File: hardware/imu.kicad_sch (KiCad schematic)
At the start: 4 parts, among them U2 BMI270

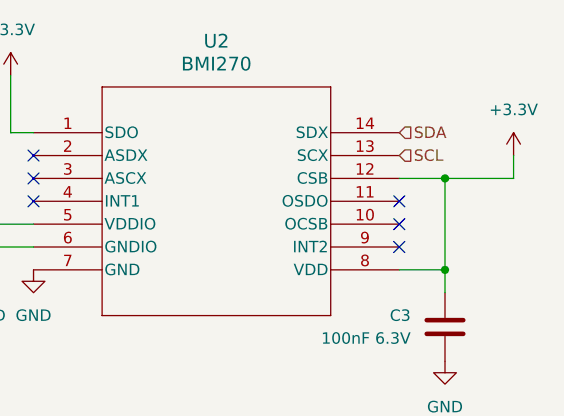
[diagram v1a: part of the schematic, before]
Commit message: lcd wires, wire direction
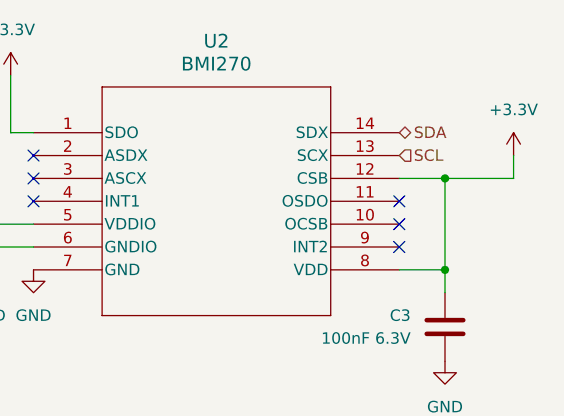
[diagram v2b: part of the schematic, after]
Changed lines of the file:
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@@
 	)
 	(hierarchical_label "SDA"
-		(shape input)
+		(shape bidirectional)
 		(at 177.8 82.55 0)
 		(fields_autoplaced yes)

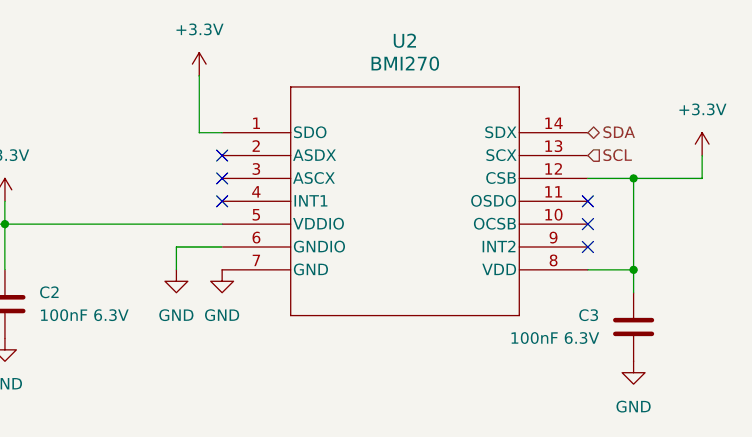
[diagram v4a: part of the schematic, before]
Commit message: Route all board
Fix CS missing for SD card
Add IMU symbol and footprint to the project lib
Finish esp32 pinswaps
Move non critical signals to the keyboard IO expander
Add power flag symbols
Fix Dpad pin type
Fix IMU pin type
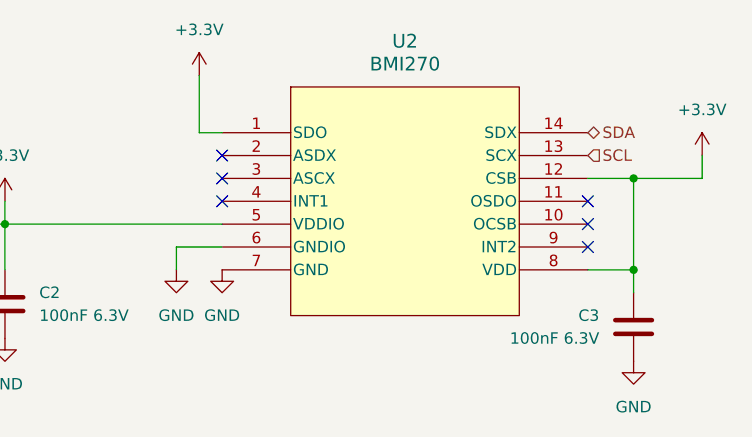
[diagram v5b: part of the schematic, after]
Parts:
- U2: footprint footprints:BMI270_BOS -> badge:BMI270_BOS; symbol 2024-05-01_14-00-02:BMI270 -> badge:BMI270
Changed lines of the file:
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@@
 	)
 	(symbol
-		(lib_id "2024-05-01_14-00-02:BMI270")
-		(at 137.16 82.55 0)
+		(lib_id "badge:BMI270")
+		(at 157.48 90.17 0)
 		(unit 1)
 		(exclude_from_sim no)
@@
 			)
 		)
-		(property "Footprint" "footprints:BMI270_BOS"
+		(property "Footprint" "badge:BMI270_BOS"
 			(at 137.16 82.55 0)
 			(effects

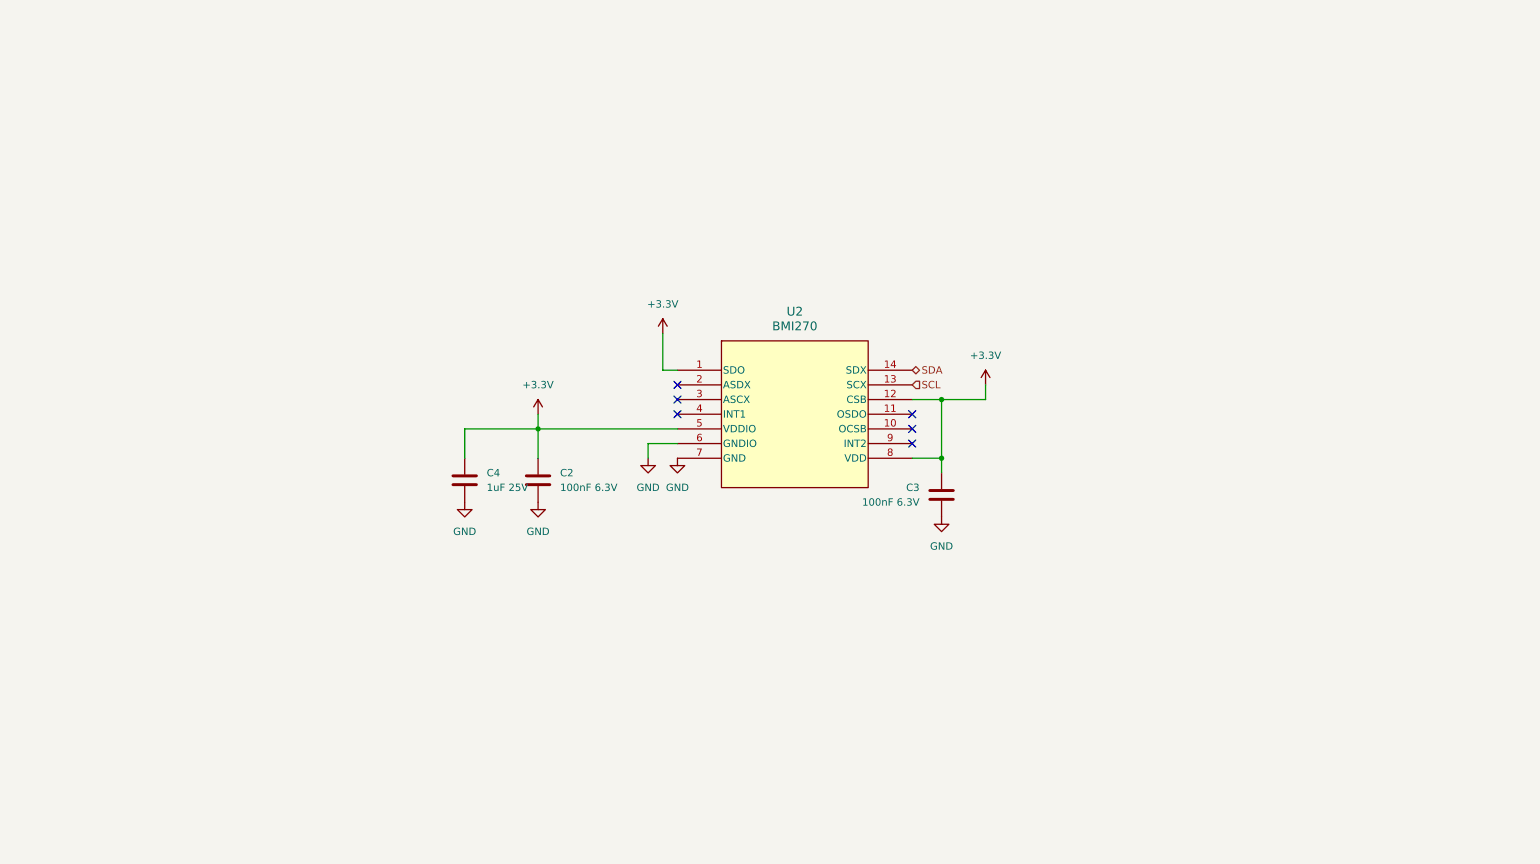
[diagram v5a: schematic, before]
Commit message: Beautified schematic, added I2C addresses
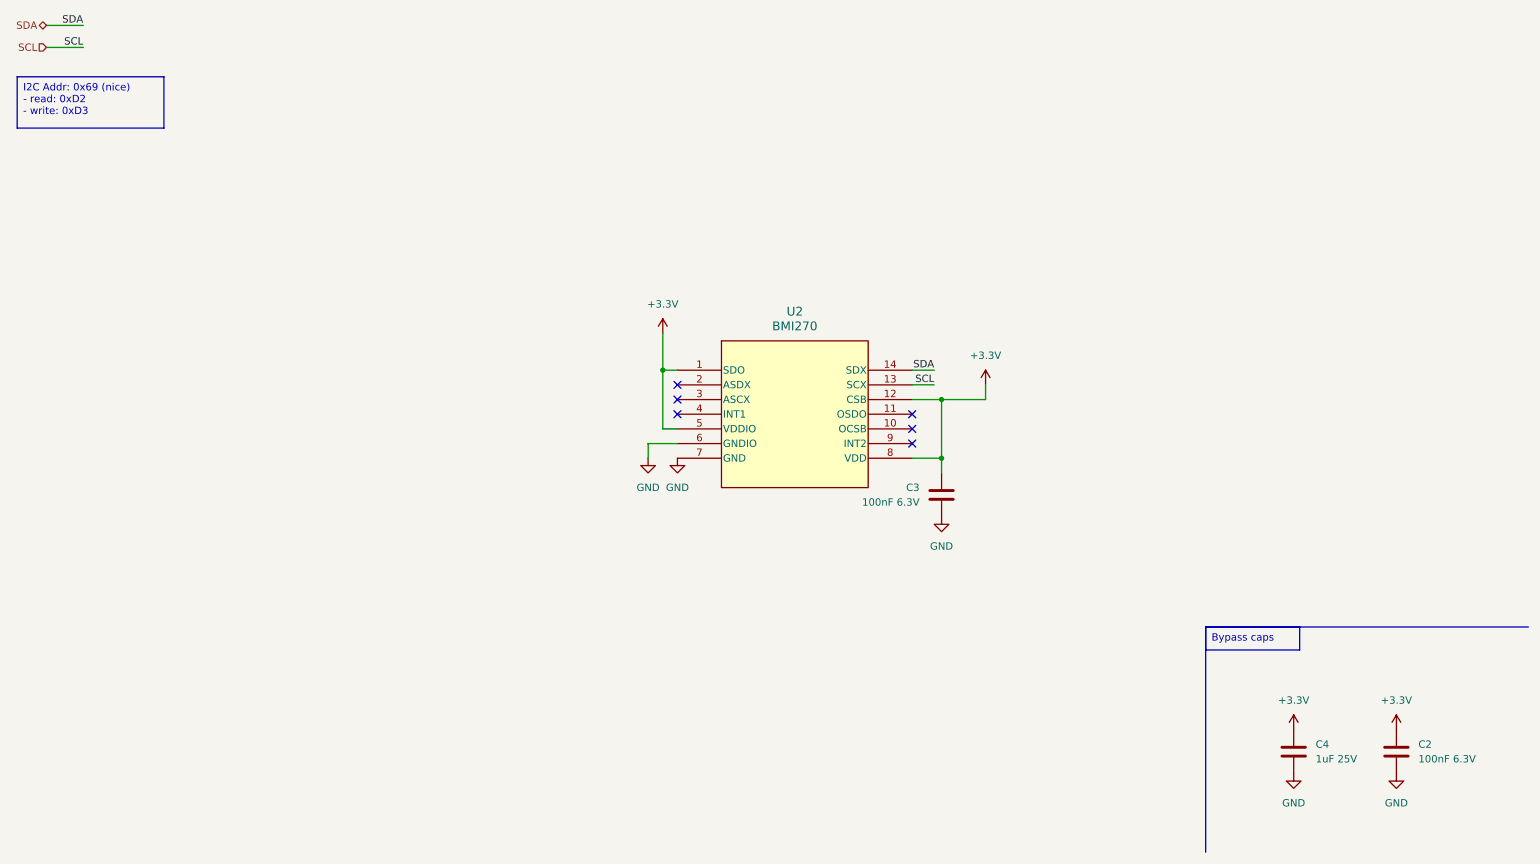
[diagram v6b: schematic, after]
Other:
- moved on the sheet: C2, C4

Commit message: update bom, correct jlcpcb rotation
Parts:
- U2: JLCPCB Rotation Offset (none) -> 180
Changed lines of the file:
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@@
+			)
+		)
+		(property "JLCPCB Rotation Offset" "180"
+			(at 157.48 90.17 0)
+			(effects
+				(font
+					(size 1.27 1.27)
+				)
+				(hide yes)
 			)
 		)
